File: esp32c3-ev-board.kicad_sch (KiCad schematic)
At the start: 63 parts, among them IC1 ESP32-C3FH4, IC2 W25Q128JVSIQ, IC3 ACS711EEXTK-31AB-T, IC4 SPX3819M5-L-3-3, J1 Battery Neg(Series), J2 Regulated Pos, J3 USB_C_Receptacle_USB2.0, J4 Conn_01x04_Pin, J5 Battery Pos, J6 Regulated Neg, SW2 SW_DPST_x2, SW3 SW_DPST_x2, U1 USBLC6-2SC6, U3 USBLC6-2SC6, Y1 40MHZ

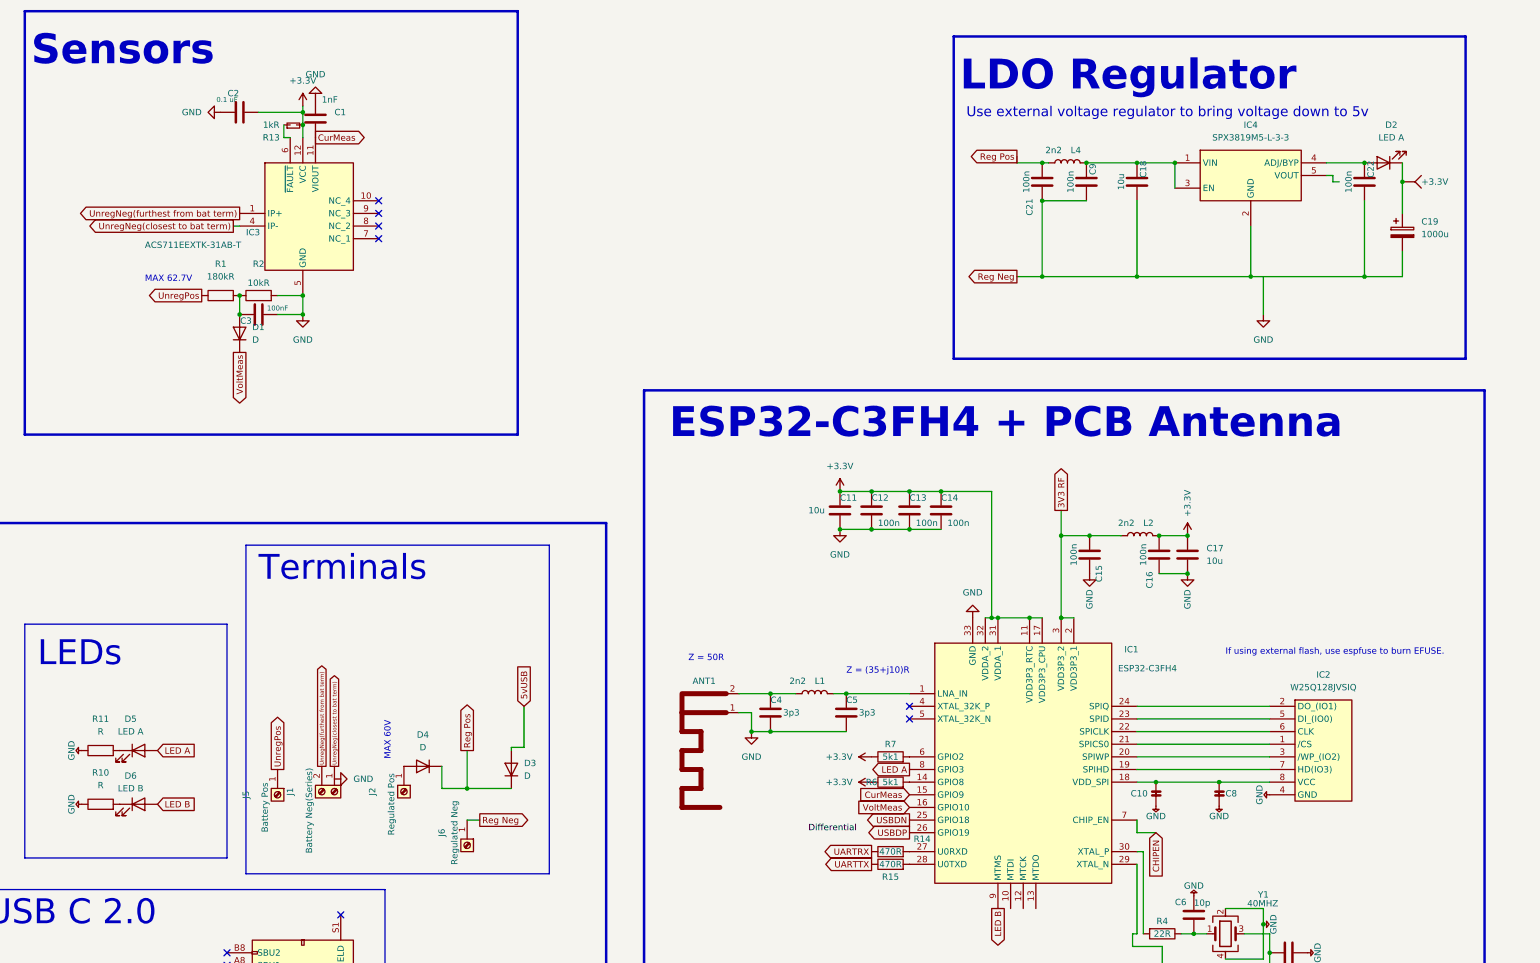
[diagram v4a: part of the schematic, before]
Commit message: Added Footprints and transfered to PCB
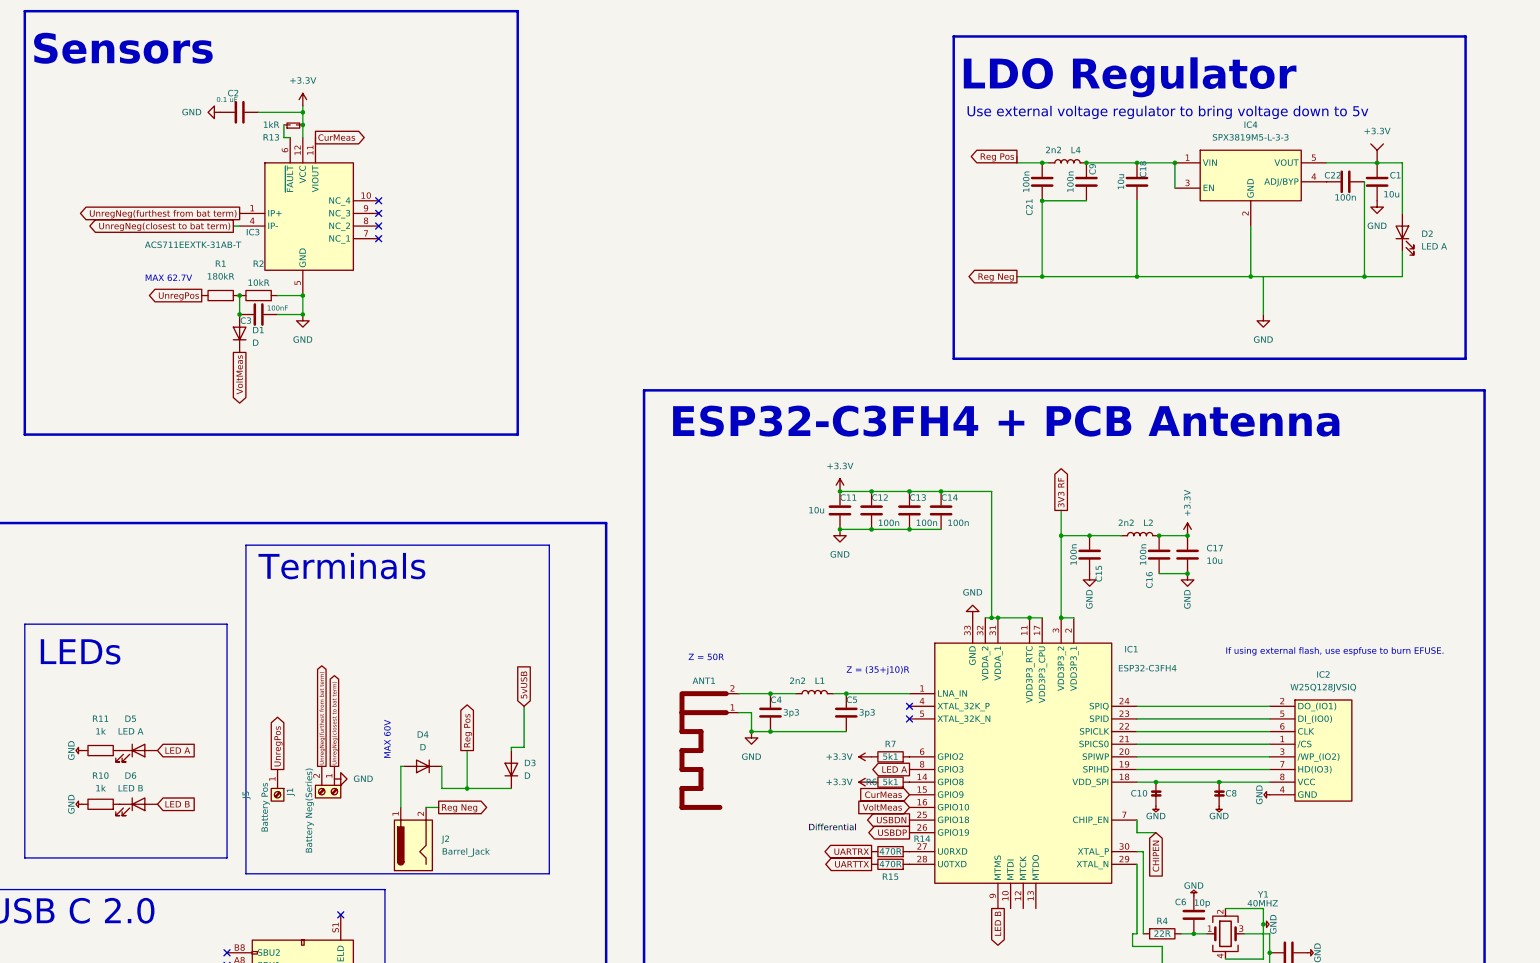
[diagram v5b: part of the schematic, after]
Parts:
- removed C19: 1000u, symbol Device:C_Polarized
- removed J2: Regulated Pos, symbol Connector:Screw_Terminal_01x01
- removed J6: Regulated Neg, symbol Connector:Screw_Terminal_01x01
- added J2: Barrel_Jack, Connector_BarrelJack:BarrelJack_CUI_PJ-063AH_Horizontal_CircularHoles, symbol Connector:Barrel_Jack
- ANT1: footprint (none) -> Library:antenna
- C1: value 1nF -> 10u; footprint (none) -> Capacitor_SMD:C_0805_2012Metric_Pad1.18x1.45mm_HandSolder
- C10, C12, C13, C14, C15, C16, C2, C20, C21, C22, C23, C24, C3, C4, C5, C6, C7, C8, C9: footprint (none) -> Capacitor_SMD:C_0603_1608Metric_Pad1.08x0.95mm_HandSolder
- C11, C17, C18: footprint (none) -> Capacitor_SMD:C_0805_2012Metric_Pad1.18x1.45mm_HandSolder
- D1, D3, D4: footprint (none) -> Diode_SMD:D_SMB_Handsoldering
- D2, D5, D6: footprint (none) -> LED_SMD:LED_0603_1608Metric_Pad1.05x0.95mm_HandSolder
- IC1: footprint QFN50P500X500X90-33N-D -> ESP32-C3FN4:QFN50P500X500X90-33N-D
- IC2: footprint SOIC127P790X216-8N -> W25Q128JVSIQ:SOIC127P790X216-8N
- IC3: footprint ACS711EEXLT31ABT -> Sensor_Current:Allegro_QFN-12-10-1EP_3x3mm_P0.5mm
- IC4: footprint SOT95P280X145-5N -> SPX3819M5-L-3-3:SOT95P280X145-5N
- J3: footprint (none) -> USB4125-GF-A-0190:USB4125GFA0190
- J4: footprint (none) -> Connector_PinHeader_2.54mm:PinHeader_1x04_P2.54mm_Vertical
- L1, L2: footprint (none) -> Inductor_SMD:L_0805_2012Metric_Pad1.05x1.20mm_HandSolder
- L4: footprint (none) -> Inductor_SMD:L_0201_0603Metric_Pad0.64x0.40mm_HandSolder
- R1, R2: footprint (none) -> Resistor_THT:R_Axial_DIN0309_L9.0mm_D3.2mm_P12.70mm_Horizontal
- R10, R11: value R -> 1k; footprint (none) -> Resistor_SMD:R_0805_2012Metric_Pad1.20x1.40mm_HandSolder
- R12, R14, R15, R16, R4, R6, R7, R8, R9: footprint (none) -> Resistor_SMD:R_0603_1608Metric_Pad0.98x0.95mm_HandSolder
- R13: footprint (none) -> Resistor_SMD:R_0805_2012Metric_Pad1.20x1.40mm_HandSolder
- SW2, SW3: footprint (none) -> FSM2JSMAATR:FSM2J_1
- Y1: footprint (none) -> Crystal:Crystal_SMD_2016-4Pin_2.0x1.6mm
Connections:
- net +3.3V: now also C1.1, D2.2 (A), IC4.5 (VOUT); no longer D2.1 (K)
- net CurMeas: no longer C1.2
- net GND: now also C1.2; no longer C1.1
- net Reg Neg: now also D2.1 (K), J2.2
- net at C22.1, IC4.4 (ADJ/BYP): no longer D2.2 (A)
- net at D4.2 (A): now also J2.1
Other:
- moved on the sheet: C22, D2

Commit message: Changed footprints
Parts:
- L4: footprint Inductor_SMD:L_0201_0603Metric_Pad0.64x0.40mm_HandSolder -> Inductor_SMD:L_0603_1608Metric_Pad1.05x0.95mm_HandSolder
- R12, R16, R4, R6, R7, R8, R9: footprint Resistor_SMD:R_0603_1608Metric_Pad0.98x0.95mm_HandSolder -> Resistor_SMD:R_1206_3216Metric_Pad1.30x1.75mm_HandSolder
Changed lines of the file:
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@@
       (effects (font (size 1.27 1.27)))
     )
-    (property "Footprint" "Resistor_SMD:R_0603_1608Metric_Pad0.98x0.95mm_HandSolder" (at 284.48 202.438 90)
+    (property "Footprint" "Resistor_SMD:R_1206_3216Metric_Pad1.30x1.75mm_HandSolder" (at 284.48 202.438 90)
       (effects (font (size 1.27 1.27)) hide)
     )
@@
       (effects (font (size 1.27 1.27)))
     )
-    (property "Footprint" "Resistor_SMD:R_0603_1608Metric_Pad0.98x0.95mm_HandSolder" (at 138.43 261.112 90)
+    (property "Footprint" "Resistor_SMD:R_1206_3216Metric_Pad1.30x1.75mm_HandSolder" (at 138.43 261.112 90)
       (effects (font (size 1.27 1.27)) hide)
     )
@@
       (effects (font (size 1.27 1.27)) (justify left))
     )
-    (property "Footprint" "Resistor_SMD:R_0603_1608Metric_Pad0.98x0.95mm_HandSolder" (at 54.102 187.96 90)
+    (property "Footprint" "Resistor_SMD:R_1206_3216Metric_Pad1.30x1.75mm_HandSolder" (at 54.102 187.96 90)
       (effects (font (size 1.27 1.27)) hide)
     )
@@
       (effects (font (size 1.27 1.27)))
     )
-    (property "Footprint" "Resistor_SMD:R_0603_1608Metric_Pad0.98x0.95mm_HandSolder" (at 138.43 262.128 90)
+    (property "Footprint" "Resistor_SMD:R_1206_3216Metric_Pad1.30x1.75mm_HandSolder" (at 138.43 262.128 90)
       (effects (font (size 1.27 1.27)) hide)
     )
@@
       (effects (font (size 1.27 1.27)) (justify left))
     )
-    (property "Footprint" "Resistor_SMD:R_0603_1608Metric_Pad0.98x0.95mm_HandSolder" (at 89.662 189.23 90)
+    (property "Footprint" "Resistor_SMD:R_1206_3216Metric_Pad1.30x1.75mm_HandSolder" (at 89.662 189.23 90)
       (effects (font (size 1.27 1.27)) hide)
     )
@@
       (effects (font (size 1.27 1.27)))
     )
-    (property "Footprint" "Resistor_SMD:R_0603_1608Metric_Pad0.98x0.95mm_HandSolder" (at 284.48 197.358 90)
+    (property "Footprint" "Resistor_SMD:R_1206_3216Metric_Pad1.30x1.75mm_HandSolder" (at 284.48 197.358 90)
       (effects (font (size 1.27 1.27)) hide)
     )
@@
       (effects (font (size 1.27 1.27)))
     )
-    (property "Footprint" "Resistor_SMD:R_0603_1608Metric_Pad0.98x0.95mm_HandSolder" (at 339.09 229.362 90)
+    (property "Footprint" "Resistor_SMD:R_1206_3216Metric_Pad1.30x1.75mm_HandSolder" (at 339.09 229.362 90)
       (effects (font (size 1.27 1.27)) hide)
     )
@@
       (effects (font (size 1.27 1.27)) (justify right))
     )
-    (property "Footprint" "Inductor_SMD:L_0201_0603Metric_Pad0.64x0.40mm_HandSolder" (at 320.04 76.2 0)
-      (effects (font (size 1.27 1.27)) hide)
-    )
+    (property "Footprint" "Inductor_SMD:L_0603_1608Metric_Pad1.05x0.95mm_HandSolder" (at 320.04 76.2 0)
+      (effects (font (size 1.27 1.27)) hide)
+    )

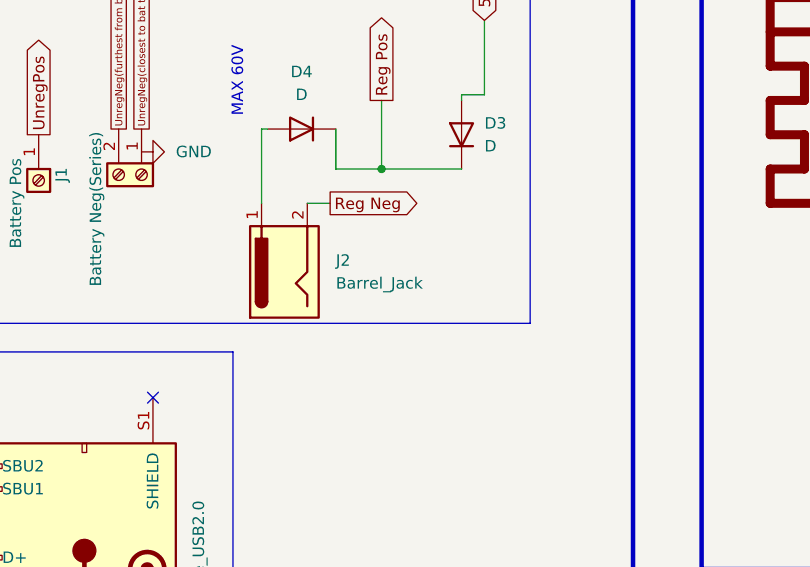
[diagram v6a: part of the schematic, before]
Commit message: Assigned new switch and DC connecter footprints
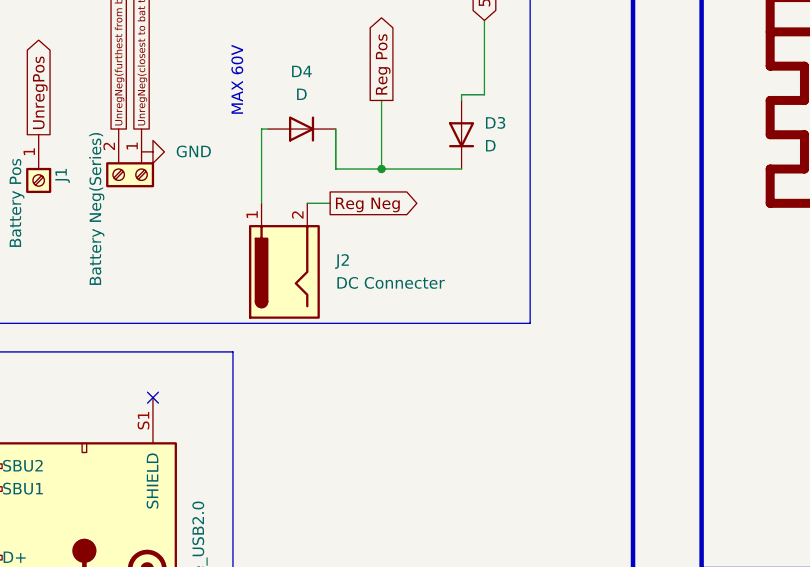
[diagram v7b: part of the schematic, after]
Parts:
- J2: value Barrel_Jack -> DC Connecter; footprint Connector_BarrelJack:BarrelJack_CUI_PJ-063AH_Horizontal_CircularHoles -> KLDX-0202-A:KLDX0202A
- SW2, SW3: footprint FSM2JSMAATR:FSM2J_1 -> SKRPANE010:SKRPADE010
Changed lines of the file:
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@@
       (effects (font (size 1.27 1.27)))
     )
-    (property "Footprint" "FSM2JSMAATR:FSM2J_1" (at 43.18 200.66 0)
+    (property "Footprint" "SKRPANE010:SKRPADE010" (at 43.18 200.66 0)
       (effects (font (size 1.27 1.27)) hide)
     )
@@
       (effects (font (size 1.27 1.27)) (justify right))
     )
-    (property "Value" "Barrel_Jack" (at 194.31 214.63 90)
-      (effects (font (size 1.27 1.27)) (justify right))
-    )
-    (property "Footprint" "Connector_BarrelJack:BarrelJack_CUI_PJ-063AH_Horizontal_CircularHoles" (at 189.611 212.09 0)
+    (property "Value" "DC Connecter" (at 194.31 214.63 90)
+      (effects (font (size 1.27 1.27)) (justify right))
+    )
+    (property "Footprint" "KLDX-0202-A:KLDX0202A" (at 189.611 212.09 0)
       (effects (font (size 1.27 1.27)) hide)
     )
@@
       (effects (font (size 1.27 1.27)))
     )
-    (property "Footprint" "FSM2JSMAATR:FSM2J_1" (at 78.74 201.93 0)
-      (effects (font (size 1.27 1.27)) hide)
-    )
+    (property "Footprint" "SKRPANE010:SKRPADE010" (at 78.74 201.93 0)
+      (effects (font (size 1.27 1.27)) hide)
+    )

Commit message: placement and routing ideas
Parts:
- added H1, H2, H3, H4: MountingHole_Pad, MountingHole:MountingHole_2.7mm_M2.5_Pad, symbol Mechanical:MountingHole_Pad
- J3: renamed from J2; value DC Connecter -> Barrel_Jack; footprint KLDX-0202-A:KLDX0202A -> (none)
- J5: renamed from J3; footprint USB4125-GF-A-0190:USB4125GFA0190 -> Connector_USB:USB_C_Receptacle_GCT_USB4105-xx-A_16P_TopMnt_Horizontal
- SW1: renamed from SW2; footprint SKRPANE010:SKRPADE010 -> FSM2JSMAATR:FSM2J_1
- SW2: renamed from SW3; footprint SKRPANE010:SKRPADE010 -> FSM2JSMAATR:FSM2J_1
- renumbered C2 to C1, C13 to C10, C14 to C11, C15 to C12, C16 to C13, C17 to C14, C4 to C15, C5 to C16, C20 to C17, C24 to C18, C10 to C19, C21 to C2, C8 to C20, C6 to C21, C7 to C22, C9 to C3, C18 to C4, C22 to C5, C1 to C6, C3 to C7, C11 to C8, C12 to C9, D2 to D1, D1 to D2, D5 to D3, D3 to D5, IC4 to IC1, IC3 to IC2, IC1 to IC3, IC2 to IC4, J5 to J2, L4 to L1, L1 to L3, R13 to R1, R14 to R10, R15 to R11, R4 to R12, R9 to R13, R8 to R14, R1 to R2, R2 to R3, R12 to R4, R16 to R5, R11 to R6, R6 to R8, R10 to R9, U3 to U2
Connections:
- net Reg Neg is gone; now on net GND: C2.2, C3.2, C4.2, C5.2, D1.1 (K), IC1.2 (GND), J3.2
- net UnregNeg(closest to bat term) is gone; now on net GND: IC2.4 (IP-), J1.1 (Pin_1)
- net 5vUSB: now also J5.A9 (VBUS), J5.B4 (VBUS), J5.B9 (VBUS)
- net GND: now also H1.1, H2.1, H3.1, H4.1; no longer J5.A9 (VBUS), J5.B4 (VBUS), J5.B9 (VBUS)
- no-connect marks 9 -> 12
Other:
- note added: "Differential"
